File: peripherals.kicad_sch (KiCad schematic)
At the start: 84 parts, among them J14 CONMMCX002-SMD-T, J5 U_FL-R-SMT-1, J7 DM3AT-SF-PEJM5, J8 WE_MicroSIM_Hinge_693022010811, Q13 BSS138-7-F, Q15 BSS138-7-F, Q8 BSS138-7-F, U10 NCP163ASN330T1G

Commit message: [#61796] Update schematics
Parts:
- C104, C105, C107: Manufacturer Yaego -> YAGEO
- C89, C90, C91, C93, C98, R127, R129, R91: now not fitted; now left out of the parts list
- C92: MPN MC0402N3R0C500CT -> C0402C309C5GACTU; Manufacturer Multicomp -> KEMET
- C97: MPN MC0402N330J500CT -> 04025A330FAT2A; Manufacturer Multicomp -> KYOCERA AVX
- D14, D15, D17, D18, D19, D44: Color (none) -> Green; Manufacturer Lite-On Inc. -> Lite-On
- E1, J14: Manufacturer Linx -> Linx Technologies
- J5: Manufacturer Hirose -> Hirose Electric; now not fitted; now left out of the parts list
- J7: Manufacturer Hirose -> Hirose Electric
- L20: Manufacturer Taiyo Yuden -> TAIYO YUDEN
- L21: value MLJ1005HXG56NETD0B -> L_56n_0.95A_0402; IMax (none) -> 0.95 A; ISat (none) -> 0.95 A; Val 56n/950mA -> 56n/0.95A
- S1, S2, S3, S4: value SW_SPST_KMR211NGLFS -> SW_KMR211NGLFS_SMD
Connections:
- net GND: now also D11.2 (A), D12.2 (A), D13.2 (A), D14.1 (C), D17.1 (C), D19.1 (C), D33.2 (A), S1.3, S2.3, S3.3; no longer D11.A, D12.A, D13.A, D14.2, D17.2, D19.2, D33.A, S1.2, S2.2, S3.2
- net LDO5_1P8: now also S4.3; no longer S4.2
- net at R95.2, S1.1: now also D11.1 (C), S1.2; no longer D11.K, S1.3
- net at R96.2, S2.1: now also D12.1 (C), S2.2; no longer D12.K, S2.3
- net at D15.1 (C): now also Q8.3 (D); no longer R103.2
- net at D15.2 (A): now also R103.2; no longer Q8.3 (D)
- net at D18.1 (C): now also Q13.3 (D); no longer R105.2
- net at D18.2 (A): now also R105.2; no longer Q13.3 (D)
- net at R102.2: now also D14.2 (A); no longer D14.1
- net at R104.2: now also D17.2 (A); no longer D17.1
- net at R106.2: now also D19.2 (A); no longer D19.1
- net at R162.2, S4.1: now also D33.1 (C), S4.2; no longer D33.K, S4.3
- net at R97.2, S3.1: now also D13.1 (C), S3.2; no longer D13.K, S3.3
- net at D44.1 (C): now also Q15.3 (D); no longer R206.2
- net at D44.2 (A): now also R206.2; no longer Q15.3 (D)
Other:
- company: (none) -> Antmicro Ltd
- moved on the sheet: C104, C97, D14, D15, D17, D18, D19, D44

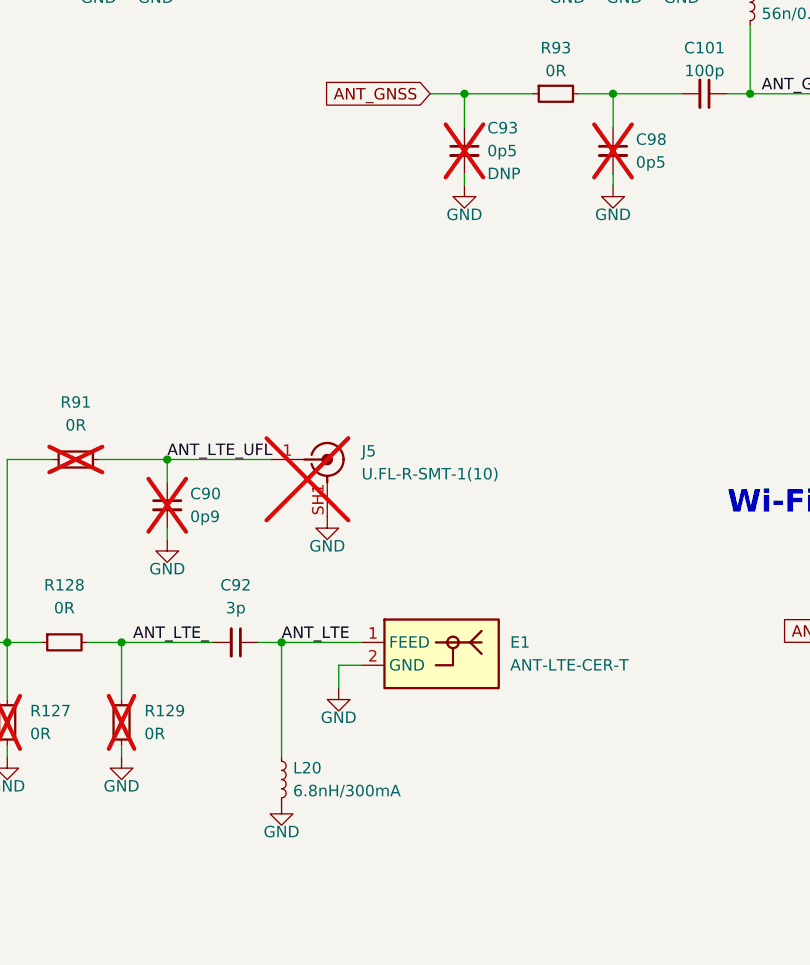
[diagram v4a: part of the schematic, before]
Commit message: [#61796] Clean ERC
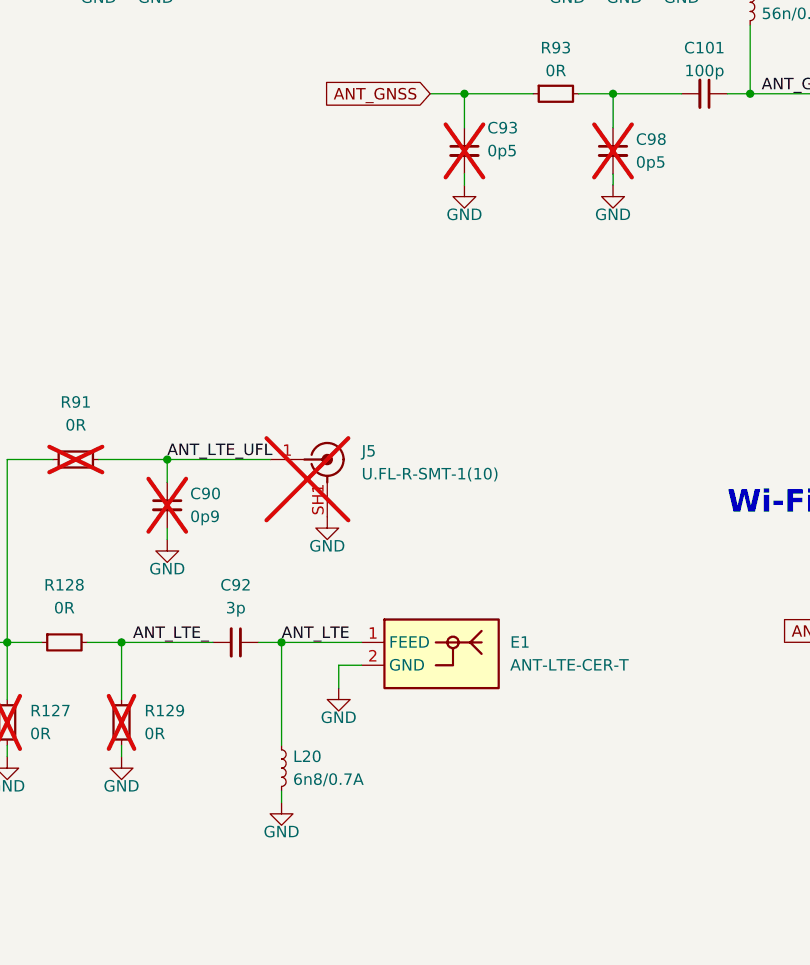
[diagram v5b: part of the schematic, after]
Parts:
- L20: value HK10056N8S-T -> L_6n8_0.7A_0402; footprint sc606-baseboard-footprints:INDC1005X55N -> antmicro-footprints:L_0402_1005Metric; symbol sc606-baseboard:HK10056N8S-T -> antmicroFixedInductors:L_6n8_0.7A_0402; IMax (none) -> 0.7 A; MPN HK10056N8S-T -> LQG15WZ6N8G02D; Manufacturer TAIYO YUDEN -> Murata; Size (none) -> 1.0x0.5; Val 6.8nH/300mA -> 6n8/0.7A
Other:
- moved on the sheet: L20
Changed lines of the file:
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@@
     (stroke (width 0) (type default))
   )
+  (wire (pts (xy 86.36 248.92) (xy 86.36 250.19))
+    (stroke (width 0) (type default))
+  )
   (wire (pts (xy 142.24 45.72) (xy 142.24 43.18))
     (stroke (width 0) (type default))
@@
     (stroke (width 0) (type default))
   )
-  (wire (pts (xy 86.36 245.11) (xy 86.36 232.41))
+  (wire (pts (xy 86.36 243.84) (xy 86.36 232.41))
     (stroke (width 0) (type default))
   )
@@
     )
     (property "DNP" "DNP" (at 109.22 180.3463 90)
-      (effects (font (size 1.27 1.27)) (justify left))
+      (effects (font (size 1.27 1.27)) (justify left) hide)
     )
     (property "License" "Apache-2.0" (at 83.82 195.58 0)
@@
     )
   )
-  (symbol (lib_id "sc606-baseboard:HK10056N8S-T") (at 86.36 245.11 270) (unit 1)
+  (symbol (lib_id "antmicroFixedInductors:L_6n8_0.7A_0402") (at 86.36 243.84 270) (unit 1)
     (in_bom yes) (on_board yes) (dnp no) (fields_autoplaced)
-    (property "Reference" "L20" (at 87.63 246.38 90)
+    (property "Reference" "L20" (at 87.63 245.11 90)
       (effects (font (size 1.27 1.27) (thickness 0.15)) (justify left))
     )
-    (property "Value" "HK10056N8S-T" (at 83.82 259.08 0)
+    (property "Value" "L_6n8_0.7A_0402" (at 60.96 259.08 0)
       (effects (font (size 1.27 1.27) (thickness 0.15)) (justify left bottom) hide)
     )
-    (property "Footprint" "sc606-baseboard-footprints:INDC1005X55N" (at 78.74 259.08 0)
+    (property "Footprint" "antmicro-footprints:L_0402_1005Metric" (at 58.42 259.08 0)
       (effects (font (size 1.27 1.27) (thickness 0.15)) (justify left bottom) hide)
     )
-    (property "Datasheet" "https://www.mouser.com/datasheet/2/396/mlci04_e-1396612.pdf" (at 76.2 259.08 0)
+    (property "Datasheet" "https://eu.mouser.com/datasheet/2/281/1/JELF243B_9117-1877420.pdf" (at 55.88 259.08 0)
       (effects (font (size 1.27 1.27) (thickness 0.15)) (justify left bottom) hide)
     )
-    (property "Manufacturer" "TAIYO YUDEN" (at 73.66 259.08 0)
+    (property "Manufacturer" "Murata" (at 76.2 259.08 0)
       (effects (font (size 1.27 1.27) (thickness 0.15)) (justify left bottom) hide)
     )
-    (property "MPN" "HK10056N8S-T" (at 71.12 259.08 0)
+    (property "MPN" "LQG15WZ6N8G02D" (at 53.34 259.08 0)
       (effects (font (size 1.27 1.27) (thickness 0.15)) (justify left bottom) hide)
     )
-    (property "Val" "6.8nH/300mA" (at 87.63 248.92 90)
+    (property "Val" "6n8/0.7A" (at 87.63 247.65 90)
       (effects (font (size 1.27 1.27) (thickness 0.15)) (justify left))
     )
-    (property "ISat" "" (at 69.85 259.08 0)
-      (effects (font (size 1.27 1.27)) (justify left) hide)
+    (property "ISat" "" (at 73.66 259.08 0)
+      (effects (font (size 1.27 1.27) (thickness 0.15)) (justify left bottom) hide)
     )
-    (property "IMax" "" (at 66.04 259.08 0)
+    (property "IMax" "0.7 A" (at 71.12 259.08 0)
       (effects (font (size 1.27 1.27) (thickness 0.15)) (justify left bottom) hide)
     )
-    (property "Size" "" (at 63.5 259.08 0)
+    (property "Size" "1.0x0.5" (at 68.58 259.08 0)
       (effects (font (size 1.27 1.27) (thickness 0.15)) (justify left bottom) hide)
     )
-    (property "Author" "Antmicro" (at 60.96 259.08 0)
+    (property "Author" "Antmicro" (at 66.04 259.08 0)
       (effects (font (size 1.27 1.27) (thickness 0.15)) (justify left bottom) hide)
     )
-    (property "License" "Apache-2.0" (at 58.42 259.08 0)
+    (property "License" "Apache-2.0" (at 63.5 259.08 0)
       (effects (font (size 1.27 1.27) (thickness 0.15)) (justify left bottom) hide)
     )

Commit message: [#61796] Update designators
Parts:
- renumbered E1 to AE1, A1 to AE2
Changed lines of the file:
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@@
   (symbol (lib_id "antmicroRFAntennas:ANT-LTE-CER-T") (at 95.25 232.41 0) (unit 1)
     (in_bom yes) (on_board yes) (dnp no) (fields_autoplaced)
-    (property "Reference" "E1" (at 111.76 232.41 0)
+    (property "Reference" "AE1" (at 111.76 232.41 0)
       (effects (font (size 1.27 1.27)) (justify left))
     )
@@
       (project "sc606-baseboard"
         (path "/d033de6c-b5da-4924-ae5b-c5bab6f8ca2c/00000000-0000-0000-0000-000061d49fde"
-          (reference "E1") (unit 1)
+          (reference "AE1") (unit 1)
         )
       )
@@
   (symbol (lib_id "antmicroRFAntennas:47948-0001") (at 182.88 231.14 0) (unit 1)
     (in_bom yes) (on_board yes) (dnp no) (fields_autoplaced)
-    (property "Reference" "A1" (at 191.77 223.52 0)
+    (property "Reference" "AE2" (at 191.77 223.52 0)
       (effects (font (size 1.27 1.27) (thickness 0.15)))
     )
@@
       (project "sc606-baseboard"
         (path "/d033de6c-b5da-4924-ae5b-c5bab6f8ca2c/00000000-0000-0000-0000-000061d49fde"
-          (reference "A1") (unit 1)
+          (reference "AE2") (unit 1)
         )
       )
